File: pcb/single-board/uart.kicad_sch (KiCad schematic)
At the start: 20 parts, among them J5 UART1, J6 UART2, J7 Serial, J8 Serial, U20 74HC688, U21 W65C51NxP, U22 74HC688, U23 W65C51NxP, Y1 1.8432 MHz, Y2 1.8432 MHz

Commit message: Further revising
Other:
- note added: "Signals are wired such that TxD <-> RxD ~{CTS} <-> ~{RTS} such that no null-modem cable is needed."
- note added: "UART"
- moved on the sheet: C25, C26, C27, J7, R7, R8, U21, U22, Y1

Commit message: Refactoring source
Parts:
- U20, U22: value 74HC688 -> CD74HC688
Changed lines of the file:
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@@
 			)
 		)
-		(property "Value" "74HC688"
+		(property "Value" "CD74HC688"
 			(at 46.99 40.386 0)
 			(effects
@@
 			)
 		)
-		(property "Value" "74HC688"
+		(property "Value" "CD74HC688"
 			(at 180.34 39.116 0)
 			(effects

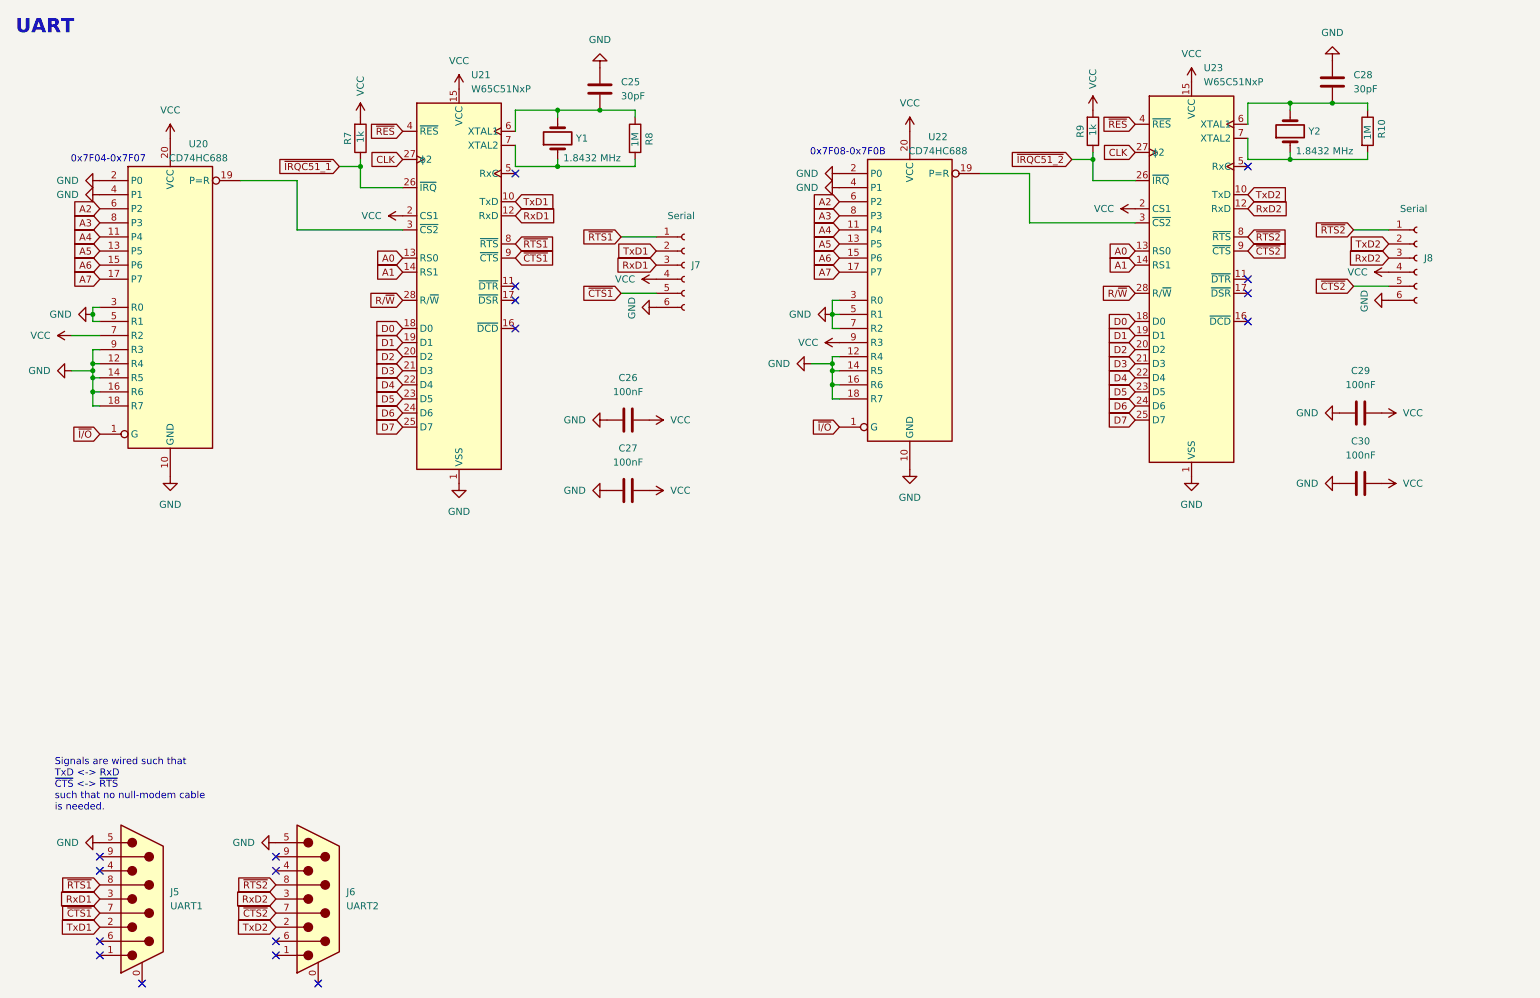
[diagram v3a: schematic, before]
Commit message: Revising single board layout
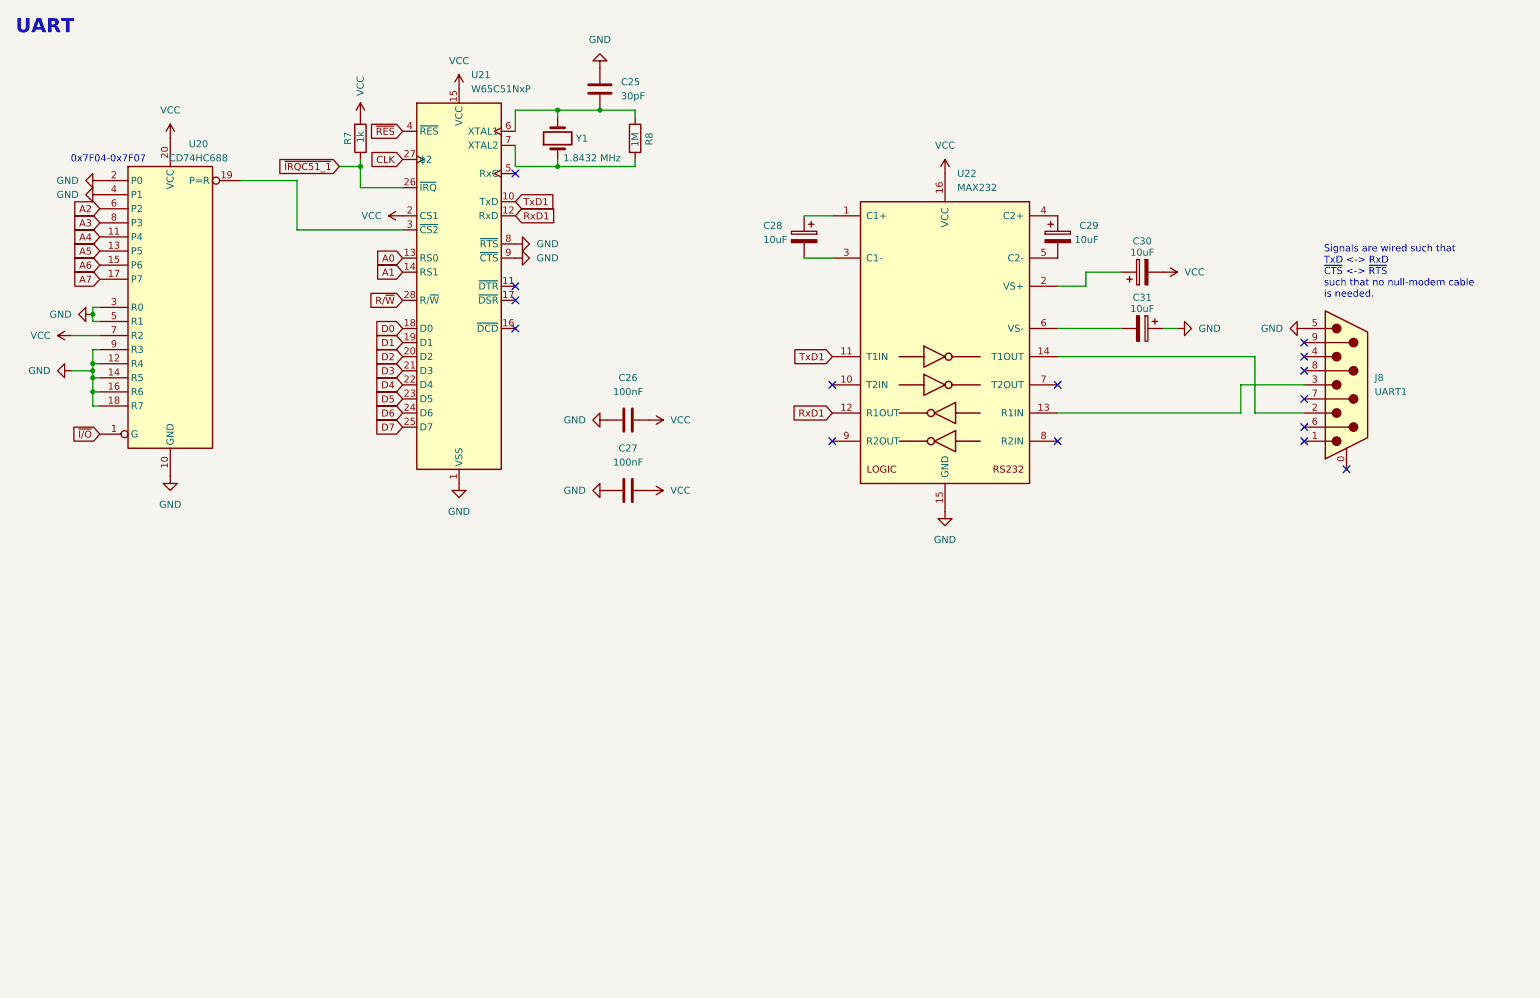
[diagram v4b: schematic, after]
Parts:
- removed C28: 30pF, Capacitor_THT:C_Disc_D5.0mm_W2.5mm_P5.00mm, symbol Device:C
- removed C29, C30: 100nF, Capacitor_THT:C_Disc_D5.0mm_W2.5mm_P5.00mm, symbol Device:C
- removed J5: UART1, Connector_Dsub:DSUB-9_Male_Horizontal_P2.77x2.84mm_EdgePinOffset4.94mm_Housed_MountingHolesOffset7.48mm, symbol Connector:DE9_Plug_MountingHoles
- removed J6: UART2, Connector_Dsub:DSUB-9_Male_Horizontal_P2.77x2.84mm_EdgePinOffset4.94mm_Housed_MountingHolesOffset7.48mm, symbol Connector:DE9_Plug_MountingHoles
- removed J7, J8: Serial, Connector_PinSocket_2.54mm:PinSocket_1x06_P2.54mm_Vertical, symbol Connector:Conn_01x06_Socket
- removed R10: 1M, Resistor_THT:R_Axial_DIN0207_L6.3mm_D2.5mm_P7.62mm_Horizontal, symbol Device:R
- removed R9: 1k, Resistor_THT:R_Axial_DIN0207_L6.3mm_D2.5mm_P7.62mm_Horizontal, symbol Device:R
- removed U22: CD74HC688, Package_DIP:DIP-20_W7.62mm_Socket, symbol 74xx:74HC688
- removed U23: W65C51NxP, Package_DIP:DIP-28_W15.24mm_Socket, symbol 65xx-library:W65C51NxP
- removed Y2: 1.8432 MHz, Crystal:Crystal_HC50_Vertical, symbol Device:Crystal
- added C28, C29, C30, C31: 10uF, Capacitor_THT:CP_Radial_D5.0mm_P2.50mm, symbol Device:C_Polarized
- added J8: UART1, Connector_Dsub:DSUB-9_Pins_Horizontal_P2.77x2.84mm_EdgePinOffset4.94mm_Housed_MountingHolesOffset4.94mm, symbol Connector:DE9_Plug_MountingHoles
- added U22: MAX232, Package_DIP:DIP-16_W7.62mm_Socket, symbol Interface_UART:MAX232
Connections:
- net ~{CTS1} is gone; now on net GND: U21.9 (~{CTS})
- net ~{RTS1} is gone; now on net GND: U21.8 (~{RTS})
- net GND: now also C31.1, J8.5, U22.15 (GND)
- net RxD1: now also U22.12 (R1OUT)
- net TxD1: now also U22.11 (T1IN)
- net VCC: now also C30.2, U22.16 (VCC)
- new net: C31.2, U22.6 (VS-)
- new net: C29.1, U22.4 (C2+)
- new net: C29.2, U22.5 (C2-)
- new net: C28.1, U22.1 (C1+)
- new net: C28.2, U22.3 (C1-)
- new net: J8.3, U22.13 (R1IN)
- new net: J8.2, U22.14 (T1OUT)
- new net: C30.1, U22.2 (VS+)
- no-connect marks 18 -> 15
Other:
- note removed: "0x7F08-0x7F0B"

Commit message: Routing
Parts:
- added C32: 100nF, Capacitor_THT:C_Disc_D5.0mm_W2.5mm_P5.00mm, symbol Device:C
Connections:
- net GND: now also C32.2
- net VCC: now also C32.1
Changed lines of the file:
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@@
+	(symbol
+		(lib_id "power:GND")
+		(at 120.65 114.3 270)
+		(unit 1)
+		(exclude_from_sim no)
+		(in_bom yes)
+		(on_board yes)
+		(dnp no)
+		(fields_autoplaced yes)
+		(property "Reference" "#PWR0172"
+			(at 114.3 114.3 0)
+			(effects
+				(font
+					(size 1.27 1.27)
+				)
+				(hide yes)
+			)
+		)
+		(property "Value" "GND"
+			(at 116.84 114.2999 90)
+			(effects
+				(font
+					(size 1.27 1.27)
+				)
+				(justify right)
+			)
+		)
+		(property "Footprint" ""
+			(at 120.65 114.3 0)
+			(effects
+				(font
+					(size 1.27 1.27)
+				)
+				(hide yes)
+			)
+		)
+		(property "Datasheet" ""
+			(at 120.65 114.3 0)
+			(effects
+				(font
+					(size 1.27 1.27)
+				)
+				(hide yes)
+			)
+		)
+		(property "Description" "Power symbol creates a global label with name \"GND\" , ground"
+			(at 120.65 114.3 0)
+			(effects
+				(font
+					(size 1.27 1.27)
+				)
+				(hide yes)
+			)
+		)
+		(pin "1"
+		)
+		(instances
+			(project "bytecradle-6502-single-board"
+				(path "/70c9e9e4-d560-4927-af97-189b3a969059/3d872660-efc1-47d1-8462-3fe65fa54b72"
+					(reference "#PWR0172")
+					(unit 1)
+				)
+			)
+		)
+	)
 	(symbol
 		(lib_id "power:GND")
@@
 				(path "/70c9e9e4-d560-4927-af97-189b3a969059/3d872660-efc1-47d1-8462-3fe65fa54b72"
 					(reference "C25")
+					(unit 1)
+				)
+			)
+		)
+	)
+	(symbol
+		(lib_id "Device:C")
+		(at 124.46 114.3 270)
+		(unit 1)
+		(exclude_from_sim no)
+		(in_bom yes)
+		(on_board yes)
+		(dnp no)
+		(fields_autoplaced yes)
+		(property "Reference" "C32"
+			(at 124.46 106.68 90)
+			(effects
+				(font
+					(size 1.27 1.27)
+				)
+			)
+		)
+		(property "Value" "100nF"
+			(at 124.46 109.22 90)
+			(effects
+				(font
+					(size 1.27 1.27)
+				)
+			)
+		)
+		(property "Footprint" "Capacitor_THT:C_Disc_D5.0mm_W2.5mm_P5.00mm"
+			(at 120.65 115.2652 0)
+			(effects
+				(font
+					(size 1.27 1.27)
+				)
+				(hide yes)
+			)
+		)
+		(property "Datasheet" "~"
+			(at 124.46 114.3 0)
+			(effects
+				(font
+					(size 1.27 1.27)
+				)
+				(hide yes)
+			)
+		)
+		(property "Description" "Unpolarized capacitor"
+			(at 124.46 114.3 0)
+			(effects
+				(font
+					(size 1.27 1.27)
+				)
+				(hide yes)
+			)
+		)
+		(pin "1"
+		)
+		(pin "2"
+		)
+		(instances
+			(project "bytecradle-6502-single-board"
+				(path "/70c9e9e4-d560-4927-af97-189b3a969059/3d872660-efc1-47d1-8462-3fe65fa54b72"
+					(reference "C32")
 					(unit 1)
 				)
@@
 					(unit 1)
 				)
+			)
+		)
+	)
+	(symbol
+		(lib_id "power:VCC")
+		(at 128.27 114.3 270)
+		(unit 1)
+		(exclude_from_sim no)
+		(in_bom yes)
+		(on_board yes)
+		(dnp no)
+		(fields_autoplaced yes)
+		(property "Reference" "#PWR0173"
+			(at 124.46 114.3 0)
+			(effects
+				(font
+					(size 1.27 1.27)
+				)
+				(hide yes)
+			)
+		)
+		(property "Value" "VCC"
+			(at 132.08 114.2999 90)
+			(effects
+				(font
+					(size 1.27 1.27)
+				)
+				(justify left)
+			)
+		)
+		(property "Footprint" ""
+			(at 128.27 114.3 0)
+			(effects
+				(font
+					(size 1.27 1.27)
+				)
+				(hide yes)
+			)
+		)
+		(property "Datasheet" ""
+			(at 128.27 114.3 0)
+			(effects
+				(font
+					(size 1.27 1.27)
+				)
+				(hide yes)
+			)
+		)
+		(property "Description" "Power symbol creates a global label with name \"VCC\""
+			(at 128.27 114.3 0)
+			(effects
+				(font
+					(size 1.27 1.27)
+				)
+				(hide yes)
+			)
+		)
+		(pin "1"
+		)
+		(instances
+			(project "bytecradle-6502-single-board"
+				(path "/70c9e9e4-d560-4927-af97-189b3a969059/3d872660-efc1-47d1-8462-3fe65fa54b72"
+					(reference "#PWR0173")
+					(unit 1)
+				)

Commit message: Initial commit bitbang SD-card routines
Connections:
- net GND: no longer U21.8 (~{RTS})
- no-connect marks 15 -> 16
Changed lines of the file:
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@@
 	)
 	(no_connect
+		(at 104.14 55.88)
+	)
+	(no_connect
 		(at 161.29 81.28)
 	)
@@
 					(unit 1)
 				)
-			)
-		)
-	)
-	(symbol
-		(lib_id "power:GND")
-		(at 104.14 55.88 90)
-		(unit 1)
-		(exclude_from_sim no)
-		(in_bom yes)
-		(on_board yes)
-		(dnp no)
-		(fields_autoplaced yes)
-		(property "Reference" "#PWR0166"
-			(at 110.49 55.88 0)
-			(effects
-				(font
-					(size 1.27 1.27)
-				)
-				(hide yes)
-			)
-		)
-		(property "Value" "GND"
-			(at 107.95 55.8799 90)
-			(effects
-				(font
-					(size 1.27 1.27)
-				)
-				(justify right)
-			)
-		)
-		(property "Footprint" ""
-			(at 104.14 55.88 0)
-			(effects
-				(font
-					(size 1.27 1.27)
-				)
-				(hide yes)
-			)
-		)
-		(property "Datasheet" ""
-			(at 104.14 55.88 0)
-			(effects
-				(font
-					(size 1.27 1.27)
-				)
-				(hide yes)
-			)
-		)
-		(property "Description" "Power symbol creates a global label with name \"GND\" , ground"
-			(at 104.14 55.88 0)
-			(effects
-				(font
-					(size 1.27 1.27)
-				)
-				(hide yes)
-			)
-		)
-		(pin "1"
-		)
-		(instances
-			(project "bytecradle-6502-single-board"
-				(path "/70c9e9e4-d560-4927-af97-189b3a969059/3d872660-efc1-47d1-8462-3fe65fa54b72"
-					(reference "#PWR0166")
-					(unit 1)
-				)
